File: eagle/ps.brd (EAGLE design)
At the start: 152.4 x 101.3 mm, 12 parts, among them J1 PIN2F061.100, J2 PIN2F061.100

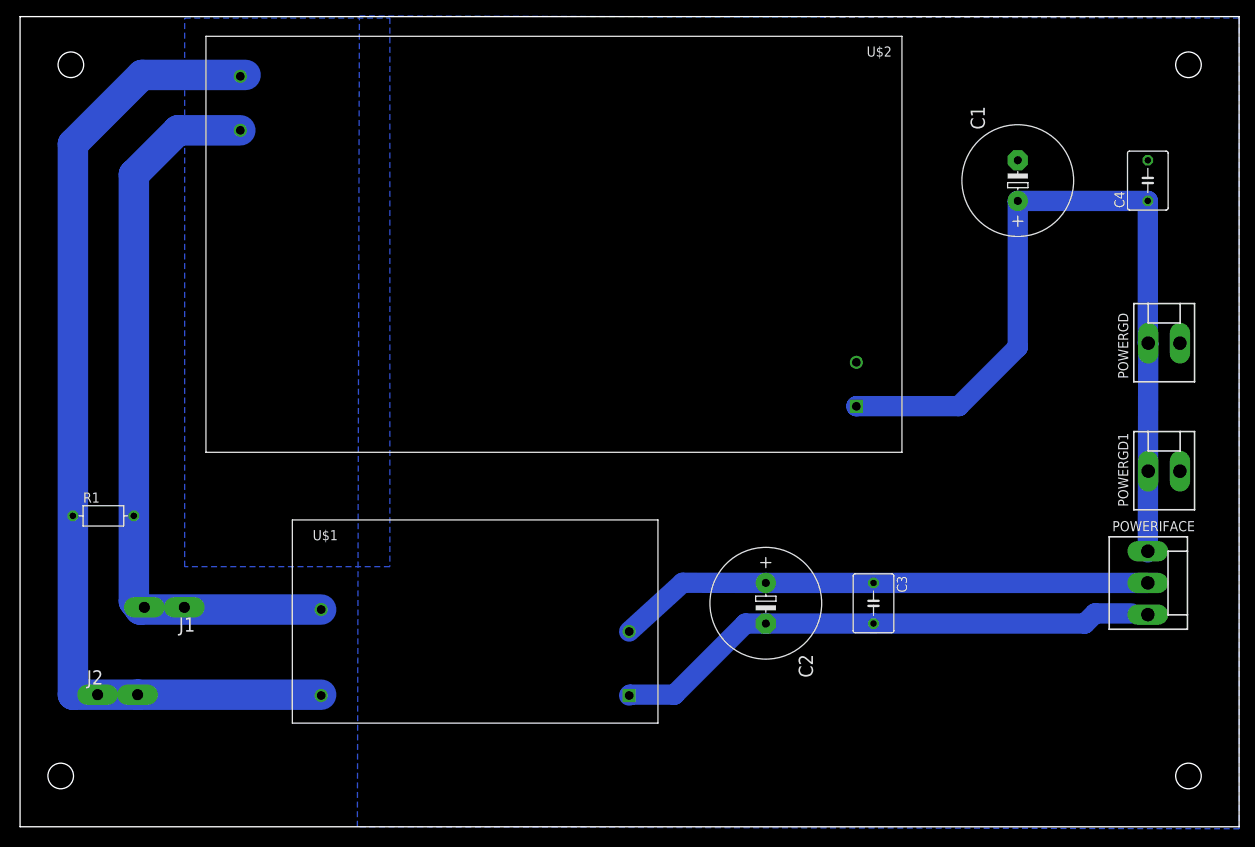
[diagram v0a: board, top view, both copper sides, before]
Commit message: 3PS, 2 1kV in parallel
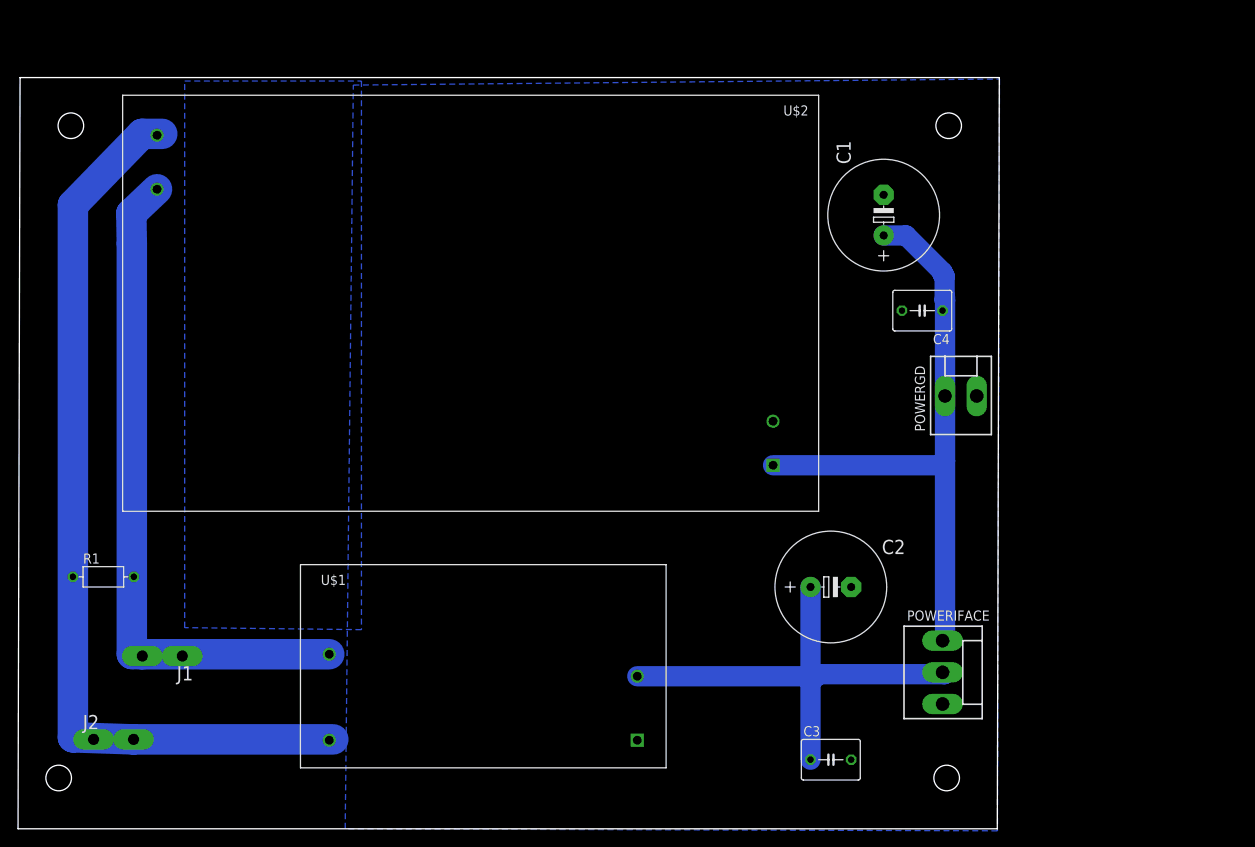
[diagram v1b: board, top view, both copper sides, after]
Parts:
- removed POWERGD1: (no value), con-molex:KK-156-2
- moved C4 32.5 mm to (112.8, 64.5), turned to 180 degrees
- moved POWERIFACE 28.0 mm to (115.3, 19.3)
- moved POWERGD 26.2 mm to (117.6, 53.8)
- moved C3 20.3 mm to (101.3, 8.38), turned to 0 degrees
- moved C1 17.3 mm to (108.0, 76.5)
- moved U$2 12.8 mm to (99.8, 91.4)
- moved C2 8.38 mm to (101.3, 30.0), turned to 0 degrees
- moved R1 7.62 mm to (10.4, 31.2)
- moved J1 6.10 mm to (17.8, 21.3)
- moved U$1 5.68 mm to (35.1, 7.37)
- moved J2 5.61 mm to (11.7, 10.9)
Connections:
- removed net +15V: C1.+, C4.1, POWERGD.1, POWERGD1.1, POWERIFACE.1, U$2.P$1
- new net +12V: C1.+, C4.1, POWERGD.1, POWERIFACE.1, U$2.P$1
- net GND: no longer POWERGD1.2
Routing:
- net +15V: track 101.8 -> 0.00 mm
- net +12V: track 0.00 -> 77.8 mm
- net GND: track 67.4 -> 0.00 mm
- net N$2: track 125.0 -> 114.0 mm
- net N$1: track 92.9 -> 84.2 mm
- net VCC: track 67.2 -> 61.3 mm
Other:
- board size 152.4 x 101.3 mm -> 122.7 x 93.9 mm

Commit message: capacitor bank
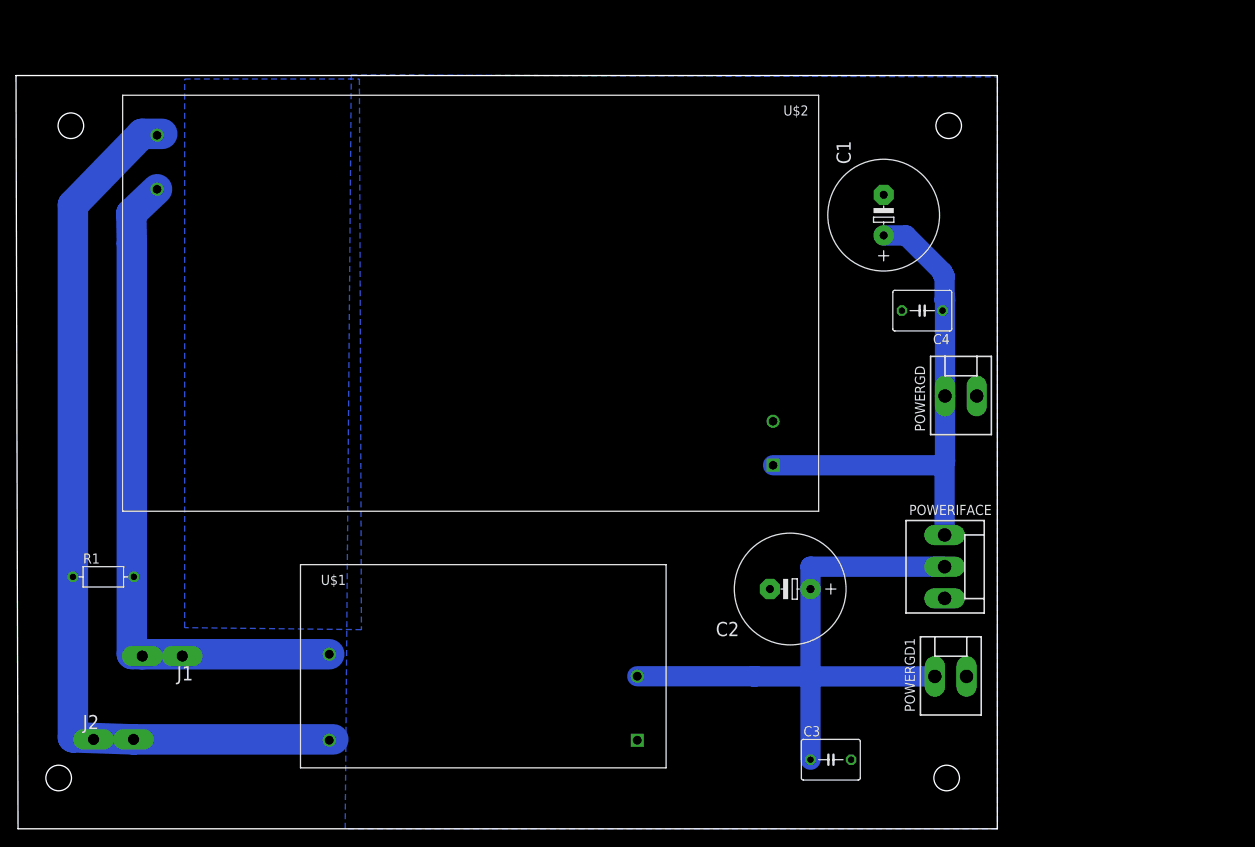
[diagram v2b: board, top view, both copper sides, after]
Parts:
- added POWERGD1: (no value), con-molex:KK-156-2
- moved POWERIFACE 13.2 mm to (115.6, 32.5)
- moved C2 5.09 mm to (96.3, 29.7), turned to 180 degrees
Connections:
- net GND: now also POWERGD1.2
- net VCC: now also POWERGD1.1
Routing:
- net VCC: track 61.3 -> 78.6 mm
- net +12V: track 77.8 -> 64.5 mm
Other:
- board size 122.7 x 93.9 mm -> 122.7 x 94.2 mm
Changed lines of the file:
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@@
 <plain>
 <wire x1="-0.254" y1="-0.254" x2="122.154" y2="-0.254" width="0" layer="20"/>
-<wire x1="122.154" y1="-0.254" x2="122.408" y2="93.65" width="0" layer="20"/>
-<wire x1="122.408" y1="93.65" x2="0" y2="93.65" width="0" layer="20"/>
-<wire x1="0" y1="93.65" x2="-0.254" y2="-0.254" width="0" layer="20"/>
+<wire x1="122.154" y1="-0.254" x2="122.154" y2="93.904" width="0" layer="20"/>
+<wire x1="122.154" y1="93.904" x2="-0.508" y2="93.904" width="0" layer="20"/>
+<wire x1="-0.508" y1="93.904" x2="-0.254" y2="-0.254" width="0" layer="20"/>
 <hole x="116.078" y="87.63" drill="3.2"/>
 <hole x="115.824" y="6.096" drill="3.2"/>
@@
 <attribute name="OC_FARNELL" value="unknown" x="117.602" y="53.848" size="1.778" layer="27" display="off"/>
 </element>
-<element name="POWERIFACE" library="con-molex" package="KK-156-3" value="" x="115.316" y="19.304" rot="R270">
-<attribute name="OC_NEWARK" value="unknown" x="115.316" y="19.304" size="1.778" layer="27" rot="R270" display="off"/>
-<attribute name="MPN" value="" x="115.316" y="19.304" size="1.778" layer="27" rot="R270" display="off"/>
-<attribute name="MF" value="" x="115.316" y="19.304" size="1.778" layer="27" rot="R270" display="off"/>
-<attribute name="OC_FARNELL" value="unknown" x="115.316" y="19.304" size="1.778" layer="27" rot="R270" display="off"/>
+<element name="POWERIFACE" library="con-molex" package="KK-156-3" value="" x="115.57" y="32.512" rot="R270">
+<attribute name="OC_NEWARK" value="unknown" x="115.57" y="32.512" size="1.778" layer="27" rot="R270" display="off"/>
+<attribute name="MPN" value="" x="115.57" y="32.512" size="1.778" layer="27" rot="R270" display="off"/>
+<attribute name="MF" value="" x="115.57" y="32.512" size="1.778" layer="27" rot="R270" display="off"/>
+<attribute name="OC_FARNELL" value="unknown" x="115.57" y="32.512" size="1.778" layer="27" rot="R270" display="off"/>
 </element>
 <element name="U$1" library="meanwell" package="IRM-05-05" value="IRM-05-05" x="35.052" y="7.366"/>
 <element name="C1" library="rcl" package="E5-13" value="" x="107.95" y="76.454" rot="R90"/>
-<element name="C2" library="rcl" package="E5-13" value="" x="101.346" y="29.972"/>
+<element name="C2" library="rcl" package="E5-13" value="" x="96.266" y="29.718" rot="R180"/>
 <element name="C3" library="rcl" package="C050-050X075" value="" x="101.346" y="8.382"/>
 <element name="C4" library="rcl" package="C050-050X075" value="" x="112.776" y="64.516" rot="R180"/>
 <element name="R1" library="varistor" package="R-7,5" value="VARISTOR-7,5" x="10.414" y="31.242"/>
 <element name="U$2" library="meanwell" package="IRM-60-12" value="IRM-60-12" x="99.822" y="91.44" rot="R180"/>
+<element name="POWERGD1" library="con-molex" package="KK-156-2" value="" x="116.332" y="18.796">
+<attribute name="OC_NEWARK" value="unknown" x="116.332" y="18.796" size="1.778" layer="27" display="off"/>
+<attribute name="MPN" value="" x="116.332" y="18.796" size="1.778" layer="27" display="off"/>
+<attribute name="MF" value="" x="116.332" y="18.796" size="1.778" layer="27" display="off"/>
+<attribute name="OC_FARNELL" value="unknown" x="116.332" y="18.796" size="1.778" layer="27" display="off"/>
+</element>
 </elements>
 <signals>
@@
 <contactref element="C3" pad="1"/>
 <contactref element="C2" pad="+"/>
-<wire x1="98.806" y1="19.07" x2="99.822" y2="19.07" width="2.54" layer="16"/>
-<wire x1="99.822" y1="19.07" x2="115.55" y2="19.07" width="2.54" layer="16"/>
-<wire x1="115.55" y1="19.07" x2="115.316" y2="19.304" width="2.54" layer="16"/>
-<wire x1="98.806" y1="29.972" x2="98.806" y2="19.304" width="2.54" layer="16"/>
-<wire x1="98.806" y1="19.304" x2="98.806" y2="19.07" width="2.54" layer="16"/>
-<wire x1="98.806" y1="19.07" x2="98.806" y2="8.382" width="2.54" layer="16"/>
-<wire x1="99.294" y1="18.542" x2="99.822" y2="19.07" width="2.54" layer="16"/>
 <contactref element="U$1" pad="+V"/>
-<wire x1="77.152" y1="18.816" x2="98.318" y2="18.816" width="2.54" layer="16"/>
-<wire x1="98.318" y1="18.816" x2="98.806" y2="19.304" width="2.54" layer="16"/>
+<contactref element="POWERGD1" pad="1"/>
+<wire x1="77.152" y1="18.816" x2="91.948" y2="18.816" width="2.54" layer="16"/>
+<wire x1="91.948" y1="18.816" x2="91.694" y2="18.796" width="2.54" layer="16"/>
+<wire x1="91.694" y1="18.796" x2="98.806" y2="18.796" width="2.54" layer="16"/>
+<wire x1="98.806" y1="18.796" x2="98.806" y2="29.718" width="2.54" layer="16"/>
+<wire x1="98.806" y1="18.796" x2="98.806" y2="8.382" width="2.54" layer="16"/>
+<wire x1="115.57" y1="32.512" x2="98.806" y2="32.512" width="2.54" layer="16"/>
+<wire x1="98.806" y1="32.512" x2="98.806" y2="29.718" width="2.54" layer="16"/>
+<wire x1="114.352" y1="18.796" x2="98.806" y2="18.796" width="2.54" layer="16"/>
 </signal>
 <signal name="+12V">
@@
 <wire x1="115.622" y1="65.786" x2="115.622" y2="66.242" width="2.54" layer="16"/>
 <wire x1="115.622" y1="53.848" x2="115.622" y2="45.72" width="2.54" layer="16"/>
-<wire x1="115.622" y1="45.72" x2="115.622" y2="23.466" width="2.54" layer="16"/>
-<wire x1="115.622" y1="23.466" x2="115.316" y2="23.264" width="2.54" layer="16"/>
 <wire x1="107.95" y1="73.914" x2="110.744" y2="73.914" width="2.54" layer="16"/>
 <wire x1="110.744" y1="73.914" x2="115.316" y2="69.342" width="2.54" layer="16"/>
@@
 <wire x1="94.122" y1="45.19" x2="115.092" y2="45.19" width="2.54" layer="16"/>
 <wire x1="115.092" y1="45.19" x2="115.622" y2="45.72" width="2.54" layer="16"/>
+<wire x1="115.622" y1="45.72" x2="115.57" y2="45.72" width="2.54" layer="16"/>
+<wire x1="115.57" y1="45.72" x2="115.57" y2="36.472" width="2.54" layer="16"/>
 <wire x1="115.622" y1="65.786" x2="115.316" y2="64.516" width="0" layer="19" extent="16-16"/>
 </signal>
@@
 <contactref element="C3" pad="2"/>
 <polygon width="0.4064" layer="16" spacing="1.4224" isolate="1.4224" thermals="no">
-<vertex x="41.656" y="92.71"/>
-<vertex x="122.428" y="93.472"/>
-<vertex x="122.174" y="-0.508"/>
+<vertex x="41.402" y="93.98"/>
+<vertex x="122.174" y="93.726"/>
+<vertex x="122.174" y="-0.254"/>
 <vertex x="40.64" y="-0.254"/>
 </polygon>
 <contactref element="U$2" pad="P$2"/>
+<contactref element="POWERGD1" pad="2"/>
 </signal>
 <signal name="N$1">
@@
 <signal name="N$3">
 <polygon width="0.4064" layer="16" spacing="1.4224" isolate="1.4224" thermals="no">
-<vertex x="20.574" y="93.218"/>
-<vertex x="42.672" y="93.218"/>
+<vertex x="20.574" y="93.472"/>
+<vertex x="42.418" y="93.472"/>
 <vertex x="42.672" y="24.638"/>
 <vertex x="20.574" y="24.892"/>
